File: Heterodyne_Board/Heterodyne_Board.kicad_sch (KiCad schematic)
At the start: 21 parts, among them J1 AVR-ISP-6, SW1 SW_SPST, U1 ATtiny85-20P, U2 TLV9054xD, U3 AP2112K-3.3, U4 LM386, U5 W25X40CLSN

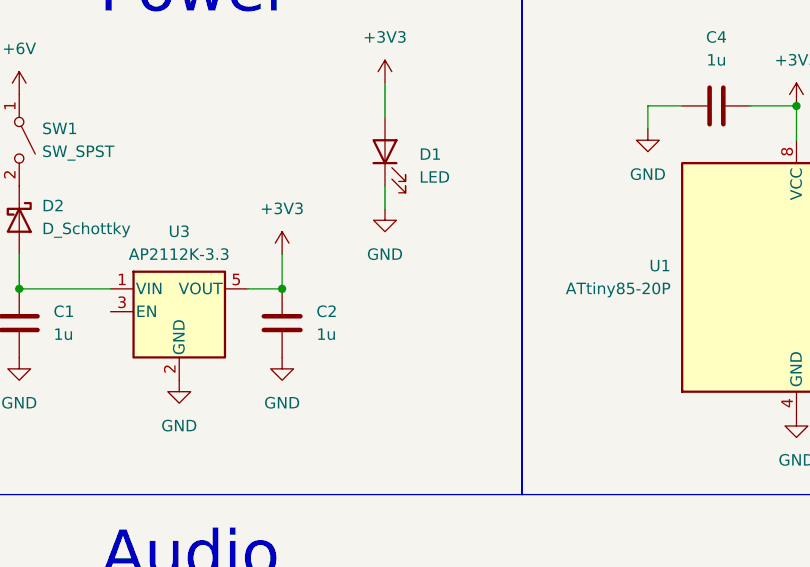
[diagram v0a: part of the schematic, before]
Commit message: Added current-limiting R on LED
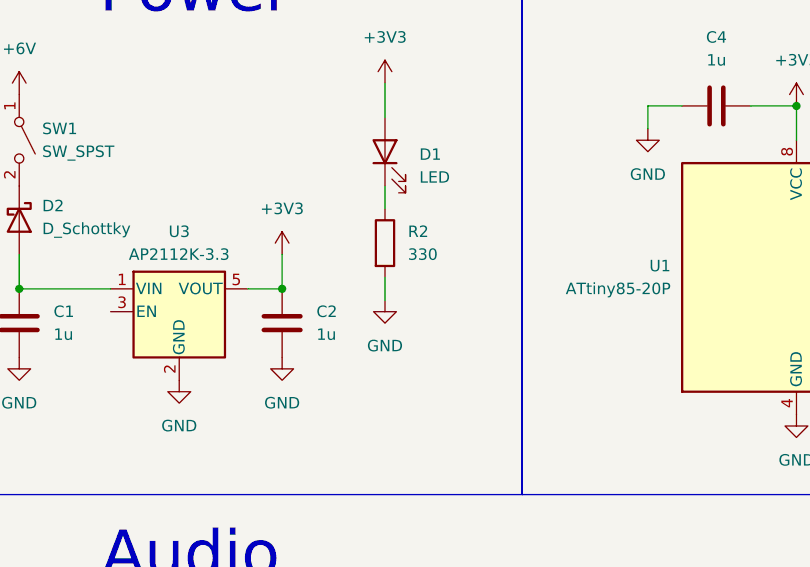
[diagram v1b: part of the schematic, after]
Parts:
- added R2: 330, symbol Device:R
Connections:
- net GND: now also R2.2; no longer D1.1 (K)
- new net: D1.1 (K), R2.1
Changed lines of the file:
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@@
+	(wire
+		(pts
+			(xy 63.5 40.64) (xy 63.5 43.18)
+		)
+		(stroke
+			(width 0)
+			(type default)
+		)
+	)
 	(wire
 		(pts
@@
 	(wire
 		(pts
+			(xy 63.5 50.8) (xy 63.5 53.34)
+		)
+		(stroke
+			(width 0)
+			(type default)
+		)
+	)
+	(wire
+		(pts
 			(xy 124.46 55.88) (xy 129.54 55.88)
 		)
@@
 		(pts
 			(xy 124.46 50.8) (xy 129.54 50.8)
-		)
-		(stroke
-			(width 0)
-			(type default)
-		)
-	)
-	(wire
-		(pts
-			(xy 63.5 40.64) (xy 63.5 43.18)
 		)
 		(stroke
@@
 	(symbol
 		(lib_id "power:GND")
-		(at 63.5 43.18 0)
+		(at 63.5 53.34 0)
 		(unit 1)
 		(exclude_from_sim no)
@@
 		(fields_autoplaced yes)
 		(property "Reference" "#PWR015"
-			(at 63.5 49.53 0)
+			(at 63.5 59.69 0)
 			(effects
 				(font
@@
 		)
 		(property "Value" "GND"
-			(at 63.5 48.26 0)
-			(effects
-				(font
-					(size 1.27 1.27)
-				)
-			)
-		)
-		(property "Footprint" ""
-			(at 63.5 43.18 0)
+			(at 63.5 58.42 0)
+			(effects
+				(font
+					(size 1.27 1.27)
+				)
+			)
+		)
+		(property "Footprint" ""
+			(at 63.5 53.34 0)
 			(effects
 				(font
@@
 		)
 		(property "Datasheet" ""
-			(at 63.5 43.18 0)
+			(at 63.5 53.34 0)
 			(effects
 				(font
@@
 		)
 		(property "Description" "Power symbol creates a global label with name \"GND\" , ground"
-			(at 63.5 43.18 0)
+			(at 63.5 53.34 0)
 			(effects
 				(font
@@
 					(unit 1)
 				)
+			)
+		)
+	)
+	(symbol
+		(lib_id "Device:R")
+		(at 63.5 46.99 0)
+		(unit 1)
+		(exclude_from_sim no)
+		(in_bom yes)
+		(on_board yes)
+		(dnp no)
+		(fields_autoplaced yes)
+		(property "Reference" "R2"
+			(at 66.04 45.7199 0)
+			(effects
+				(font
+					(size 1.27 1.27)
+				)
+				(justify left)
+			)
+		)
+		(property "Value" "330"
+			(at 66.04 48.2599 0)
+			(effects
+				(font
+					(size 1.27 1.27)
+				)
+				(justify left)
+			)
+		)
+		(property "Footprint" ""
+			(at 61.722 46.99 90)
+			(effects
+				(font
+					(size 1.27 1.27)
+				)
+				(hide yes)
+			)
+		)
+		(property "Datasheet" "~"
+			(at 63.5 46.99 0)
+			(effects
+				(font
+					(size 1.27 1.27)
+				)
+				(hide yes)
+			)
+		)
+		(property "Description" "Resistor"
+			(at 63.5 46.99 0)
+			(effects
+				(font
+					(size 1.27 1.27)
+				)
+				(hide yes)
+			)
+		)
+		(pin "1"
+		)
+		(pin "2"
+		)
+		(instances
+			(project "Heterodyne_Board"
+				(path "/bcb6d128-b2b2-45d9-80e5-2a1305aaf770"
+					(reference "R2")
+					(unit 1)
+				)

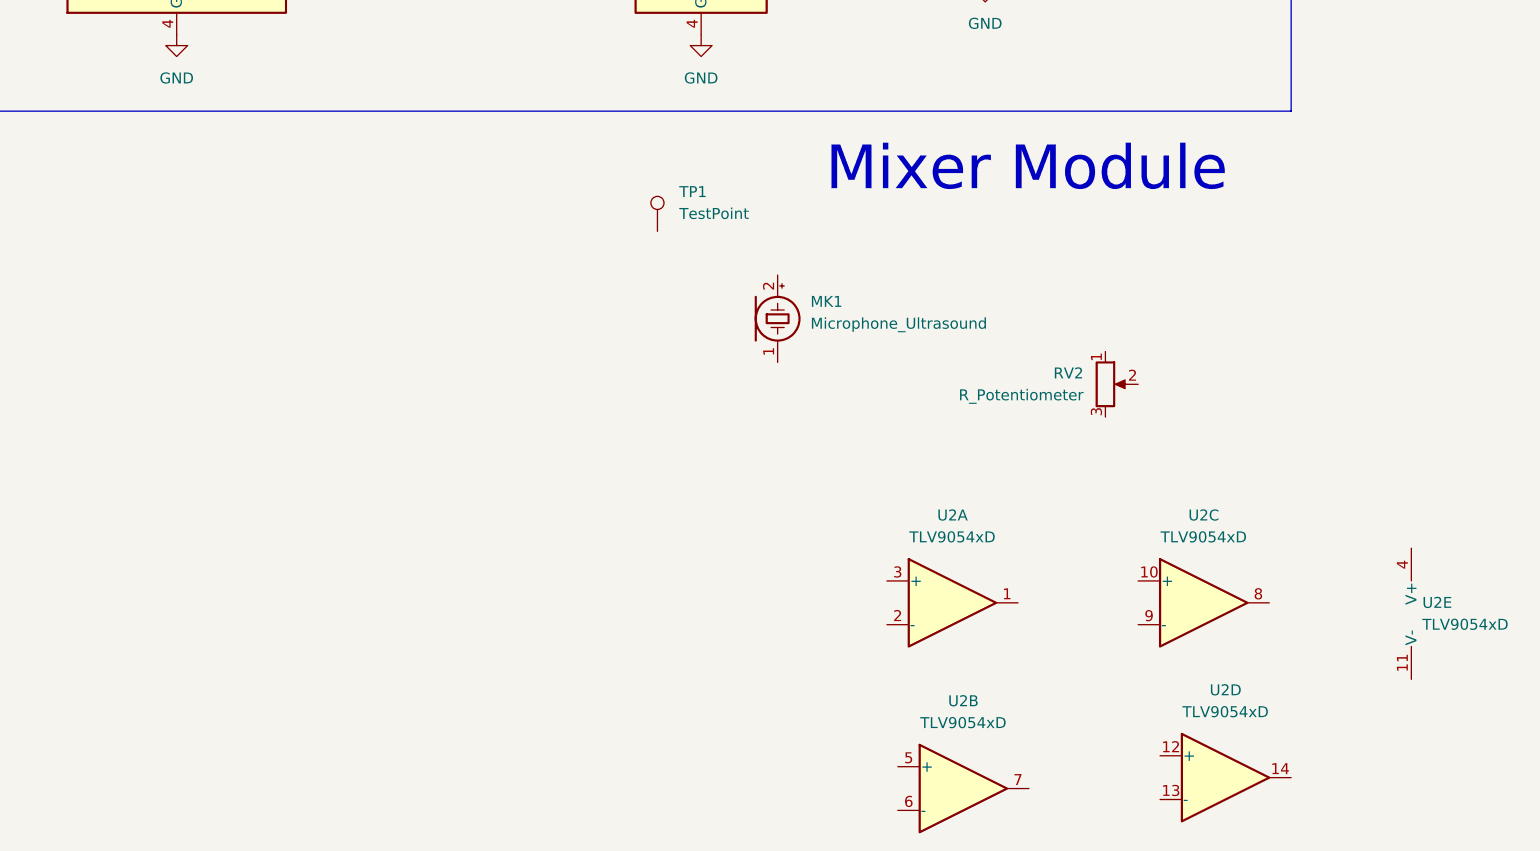
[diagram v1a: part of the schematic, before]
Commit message: PreAmp Completed
Finished schematic of Microphone output preamp and journal entry pre TA meeting
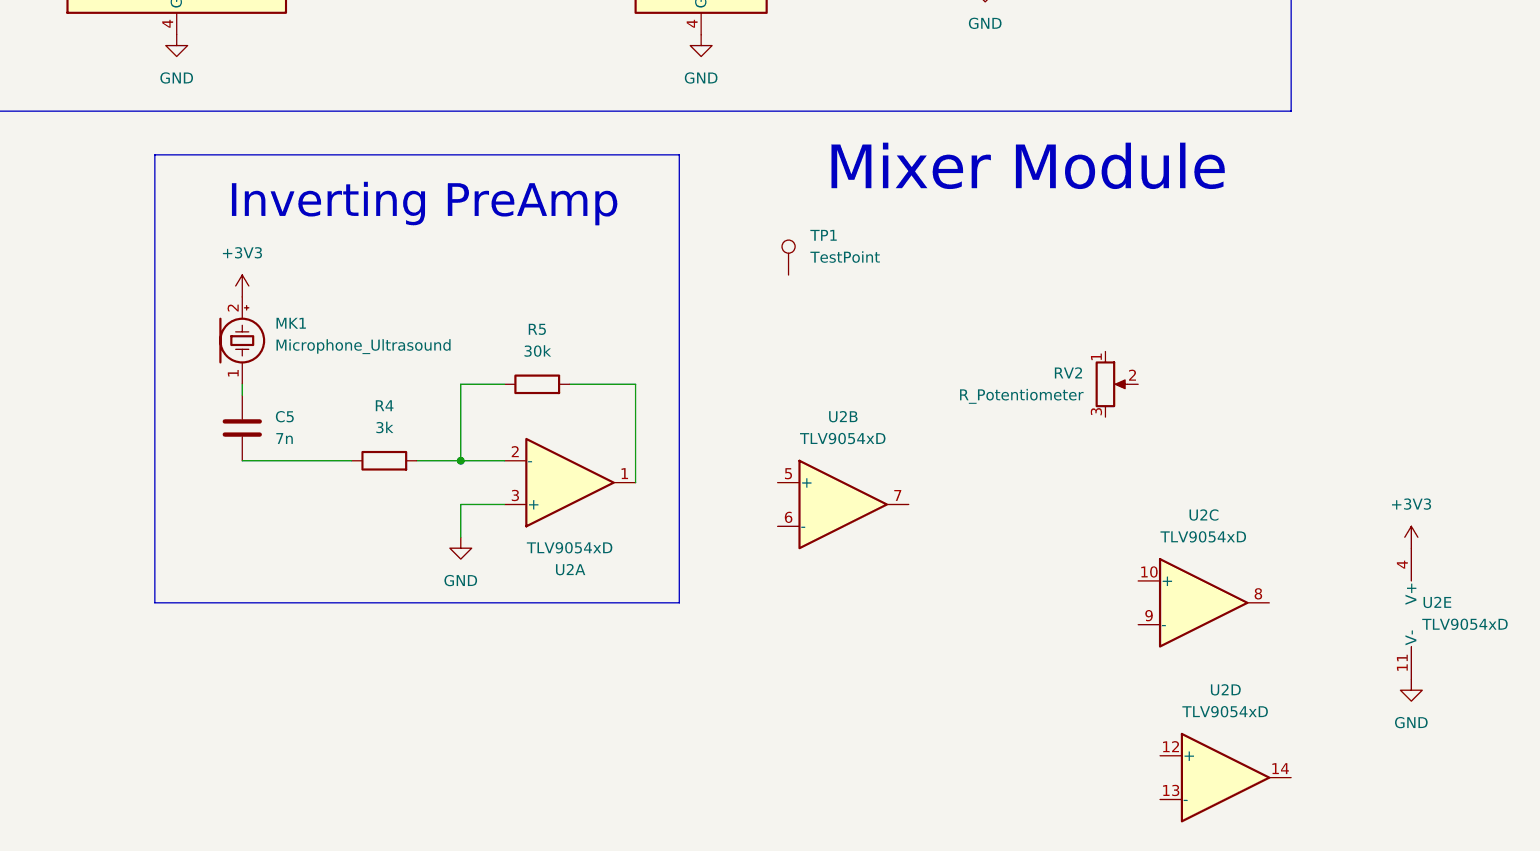
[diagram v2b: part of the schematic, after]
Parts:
- added C5: 7n, symbol Device:C
- added R4: 3k, symbol Device:R
- added R5: 30k, symbol Device:R
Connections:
- net +3V3: now also MK1.2 (+), U2.4 (V+)
- net GND: now also U2.11 (V-), U2.3 (+)
- net at MK1.1 (-): now also C5.1
- net at U2.1: now also R5.2
- net at U2.2 (-): now also R4.2, R5.1
- new net: C5.2, R4.1
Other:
- note added: "Inverting PreAmp"
- moved on the sheet: MK1, TP1, U2A, U2B

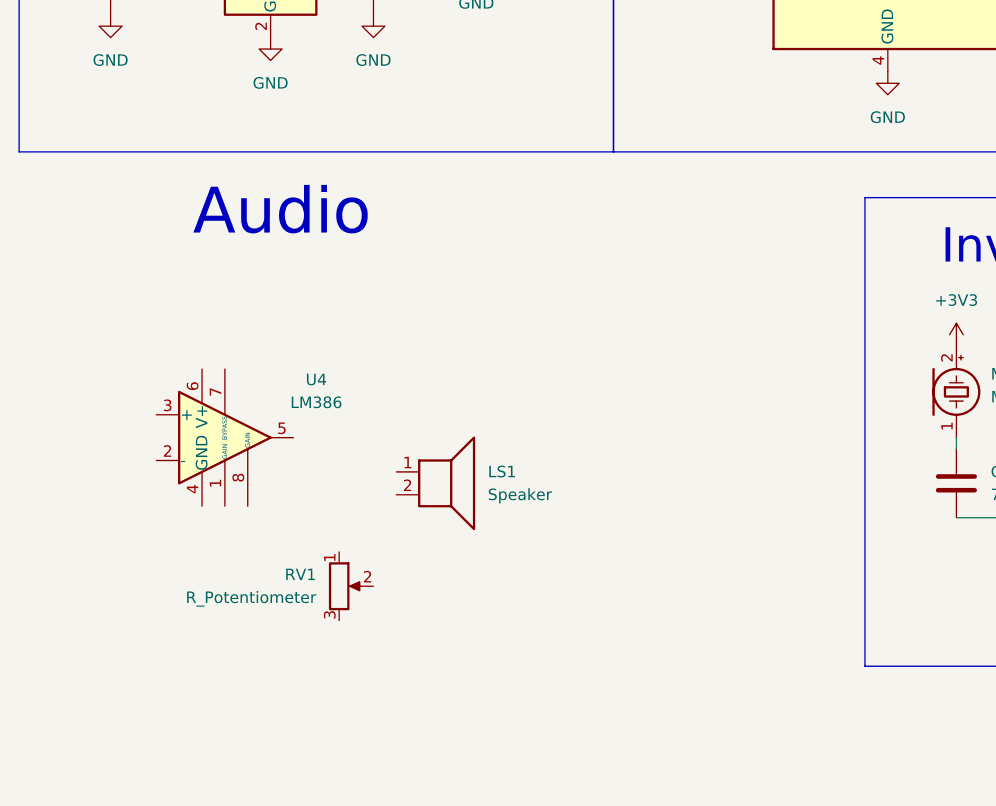
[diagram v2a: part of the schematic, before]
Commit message: Finished Speaker and Audio Amp Design
and did journal entry
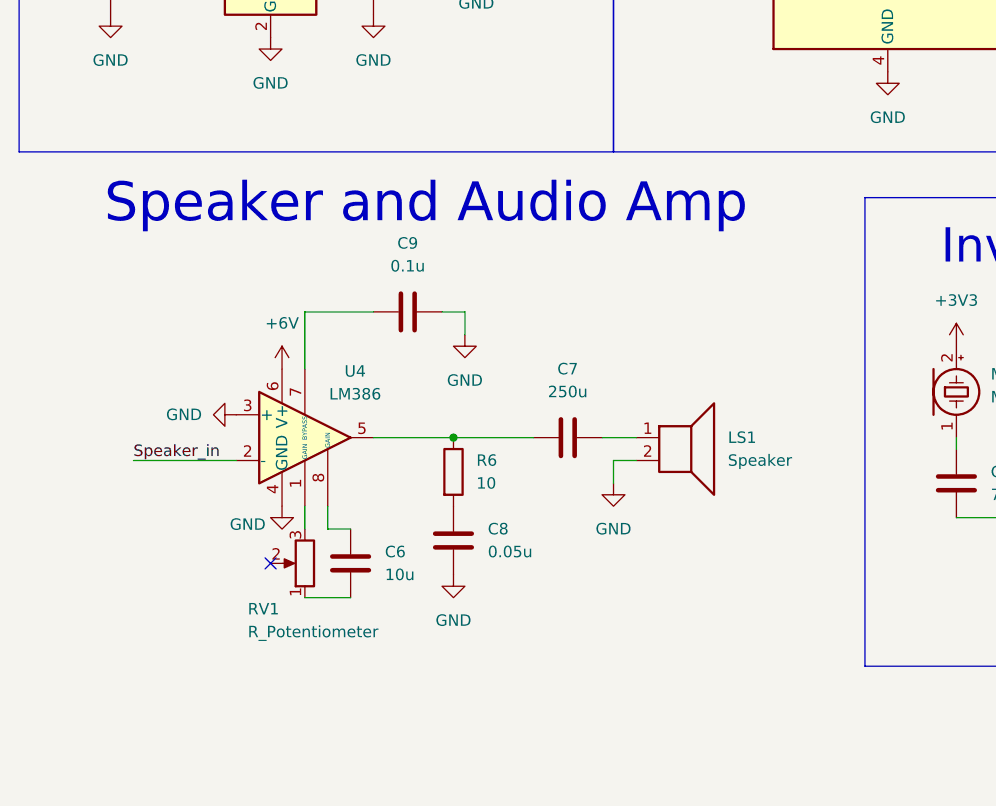
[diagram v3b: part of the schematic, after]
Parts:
- added C6: 10u, symbol Device:C
- added C7: 250u, symbol Device:C
- added C8: 0.05u, symbol Device:C
- added C9: 0.1u, symbol Device:C
- added R6: 10, symbol Device:R
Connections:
- net +6V: now also U4.6 (V+)
- net GND: now also LS1.2, U4.3 (+), U4.4 (GND), C8.1, C9.2
- net at LS1.1: now also C7.2
- net at RV1.1: now also C6.2
- net at RV1.3: now also U4.1 (GAIN)
- net Speaker_in: now reaches U4.2 (-)
- net at U4.5: now also C7.1, R6.1
- net at U4.7 (BYPASS): now also C9.1
- net at U4.8 (GAIN): now also C6.1
- new net: C8.2, R6.2
- no-connect marks 0 -> 1
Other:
- note added: "Speaker and Audio Amp"
- note removed: "Audio"
- moved on the sheet: LS1, RV1, U4

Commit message: pushing schematic so evan can see
lololol
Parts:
- added C10, C11, C12: 1u, symbol Device:C
- added R7: 996, symbol Device:R
- added R8: 1k, symbol Device:R
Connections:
- net +3V3: now also U2.3 (+), U2.9 (-), C12.2, R7.2; no longer U2.4 (V+)
- net +6V: now also U2.4 (V+)
- net GND: no longer U2.3 (+)
- net at RV2.1: now also U2.7, C10.2
- net at RV2.3: now also U2.10 (+), C11.1
- net at U2.5 (+): now also C10.1, R7.1
- net at U2.6 (-): now also C12.1, R8.1
- net Osci_out: now reaches TP1.1
- net Osci_out: now also U2.8, C11.2, R8.2
- no-connect marks 1 -> 2
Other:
- note added: "Mixer"
- note added: "Oscillator"
- note removed: "Mixer Module"
- moved on the sheet: RV2, TP1, U2B, U2C, U2D, U2E

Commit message: inverted op amp for team captain
team captain as a role is not confirmed. we may make Evan the court jester
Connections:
- net +3V3: now also U2.10 (+); no longer U2.9 (-)
- net at C11.1, RV2.3: now also U2.9 (-); no longer U2.10 (+)
- net at C10.1, R7.1: now also U2.6 (-); no longer U2.5 (+)
- net at C12.1, R8.1: now also U2.5 (+); no longer U2.6 (-)
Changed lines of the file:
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@@
 	)
 	(junction
-		(at 207.01 111.76)
+		(at 187.96 109.22)
 		(diameter 0)
 		(color 0 0 0 0)
 	)
 	(junction
-		(at 187.96 109.22)
+		(at 250.19 114.3)
 		(diameter 0)
 		(color 0 0 0 0)
 	)
 	(junction
-		(at 250.19 114.3)
+		(at 207.01 111.76)
 		(diameter 0)
 		(color 0 0 0 0)
@@
 		(lib_id "Amplifier_Operational:TLV9054xD")
 		(at 199.39 111.76 0)
+		(mirror x)
 		(unit 2)
 		(exclude_from_sim no)
@@
 		(on_board yes)
 		(dnp no)
-		(fields_autoplaced yes)
 		(property "Reference" "U2"
-			(at 199.39 101.6 0)
+			(at 199.136 105.918 0)
 			(effects
 				(font
@@
 		)
 		(property "Value" "TLV9054xD"
-			(at 199.39 104.14 0)
+			(at 199.136 103.378 0)
 			(effects
 				(font
@@
 		)
 		(property "Footprint" "Package_SO:SOIC-14_3.9x8.7mm_P1.27mm"
-			(at 198.12 109.22 0)
+			(at 198.12 114.3 0)
 			(effects
 				(font
@@
 		)
 		(property "Datasheet" "https://www.ti.com/lit/ds/symlink/tlv9054.pdf"
-			(at 201.93 124.46 0)
+			(at 201.93 99.06 0)
 			(effects
 				(font
@@
 		)
 		(property "Description" "Quad RRIO Operational Amplifiers, 15V/us slew rate, 33uVos, 5MHz GBW, SOIC-14"
-			(at 201.93 121.92 0)
+			(at 201.93 101.6 0)
 			(effects
 				(font
@@
 		(lib_id "Amplifier_Operational:TLV9054xD")
 		(at 242.57 114.3 0)
+		(mirror x)
 		(unit 3)
 		(exclude_from_sim no)
@@
 		(on_board yes)
 		(dnp no)
-		(fields_autoplaced yes)
 		(property "Reference" "U2"
-			(at 242.57 104.14 0)
+			(at 243.078 108.966 0)
 			(effects
 				(font
@@
 		)
 		(property "Value" "TLV9054xD"
-			(at 242.57 106.68 0)
+			(at 243.078 106.426 0)
 			(effects
 				(font
@@
 		)
 		(property "Footprint" "Package_SO:SOIC-14_3.9x8.7mm_P1.27mm"
-			(at 241.3 111.76 0)
+			(at 241.3 116.84 0)
 			(effects
 				(font
@@
 		)
 		(property "Datasheet" "https://www.ti.com/lit/ds/symlink/tlv9054.pdf"
-			(at 245.11 127 0)
+			(at 245.11 101.6 0)
 			(effects
 				(font
@@
 		)
 		(property "Description" "Quad RRIO Operational Amplifiers, 15V/us slew rate, 33uVos, 5MHz GBW, SOIC-14"
-			(at 245.11 124.46 0)
+			(at 245.11 104.14 0)
 			(effects
 				(font

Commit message: what a greeeeaaat work
letsa go!
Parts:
- added C13: 16n, symbol Device:C
- added R10, R11: 0, symbol Device:R
- added R12: 1k, symbol Device:R
- added R9: 10k, symbol Device:R
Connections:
- net +3V3: now also U2.12 (+), C13.2
- net +5V: now also D3.2 (A); no longer D3.1 (K)
- net Osci_out: now also R11.1
- net Speaker_in: now also C13.1, R12.2
- net at J1.2 (VCC): now also D3.1 (K); no longer D3.2 (A)
- net at C1.1, U3.1 (VIN): now also D2.1 (K), U3.3 (EN); no longer D2.2 (A)
- net at SW1.2 (B): now also D2.2 (A); no longer D2.1 (K)
- net Mic_out: now reaches R5.2, U2.1
- net Mic_out: now also R10.1
- net at U2.13 (-): now also R10.2, R11.2, R9.1
- net at U2.14: now also R12.1, R9.2
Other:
- moved on the sheet: C10, C11, C12, C3, C4, D2, D3, J1, R1, R3, R7, R8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
